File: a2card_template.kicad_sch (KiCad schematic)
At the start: 19 parts, among them U1 74LS00, U10 PLCCZ80, U14 74LS367, U15 74LS373, U16 74LS367, U17 74LS367, U3 74LS32, U5 74LS74, U6 74LS74, U7 74LS86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

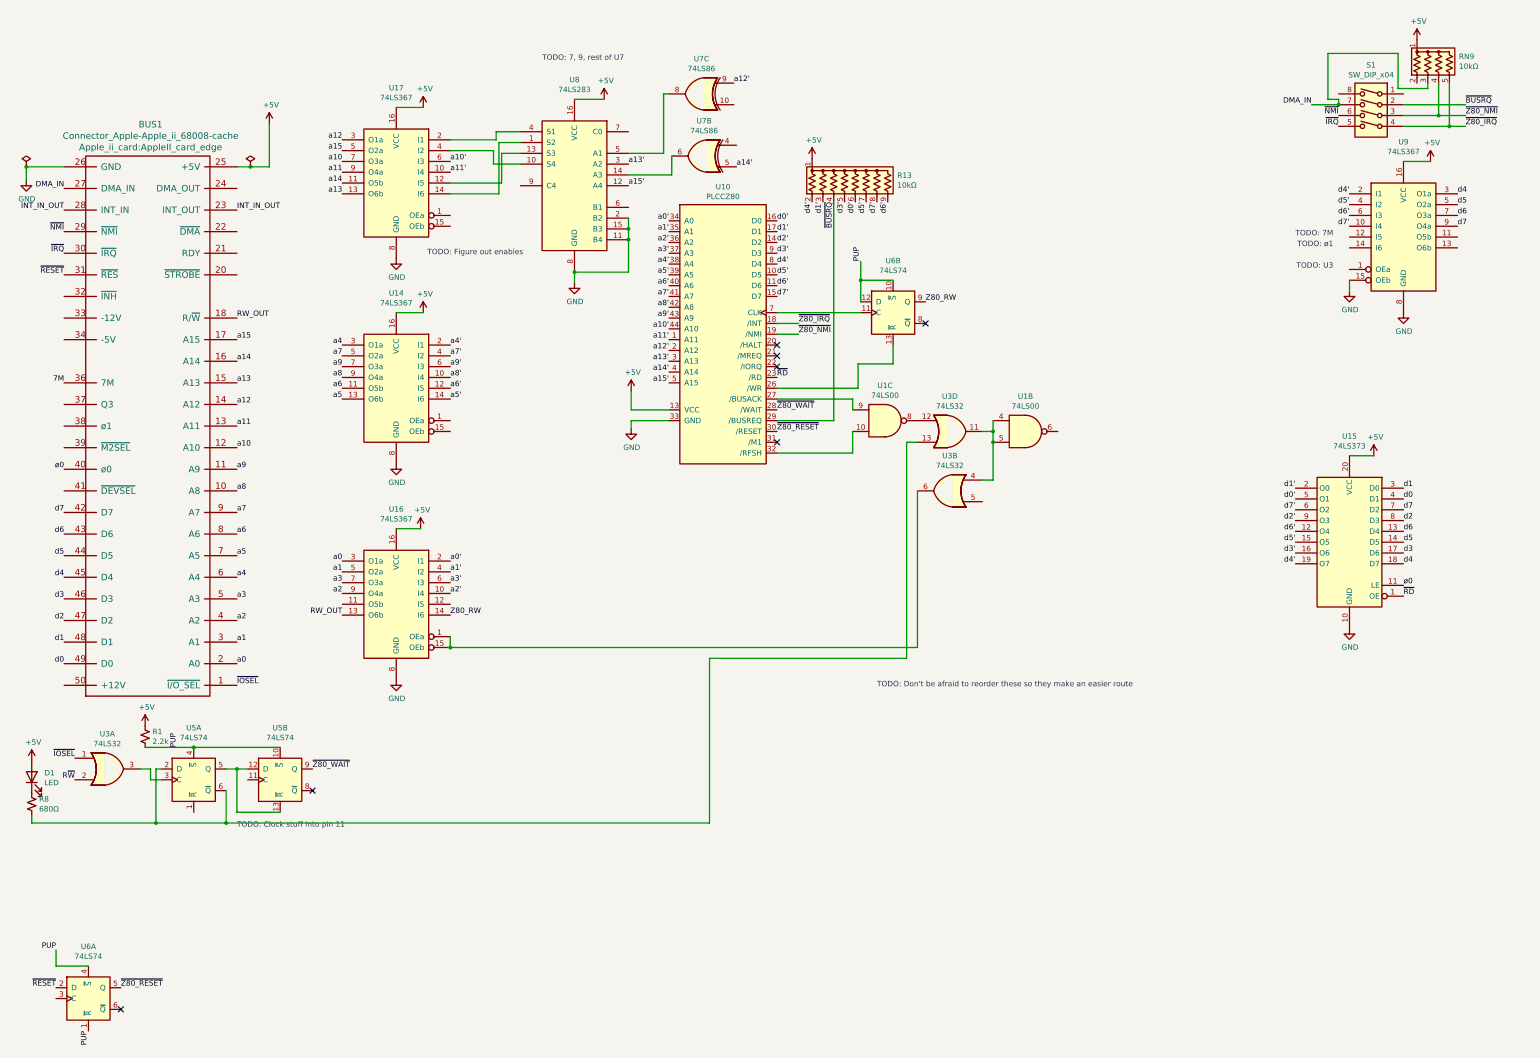
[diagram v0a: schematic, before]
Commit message: Add partial 74367 symbol, populate top row of schem
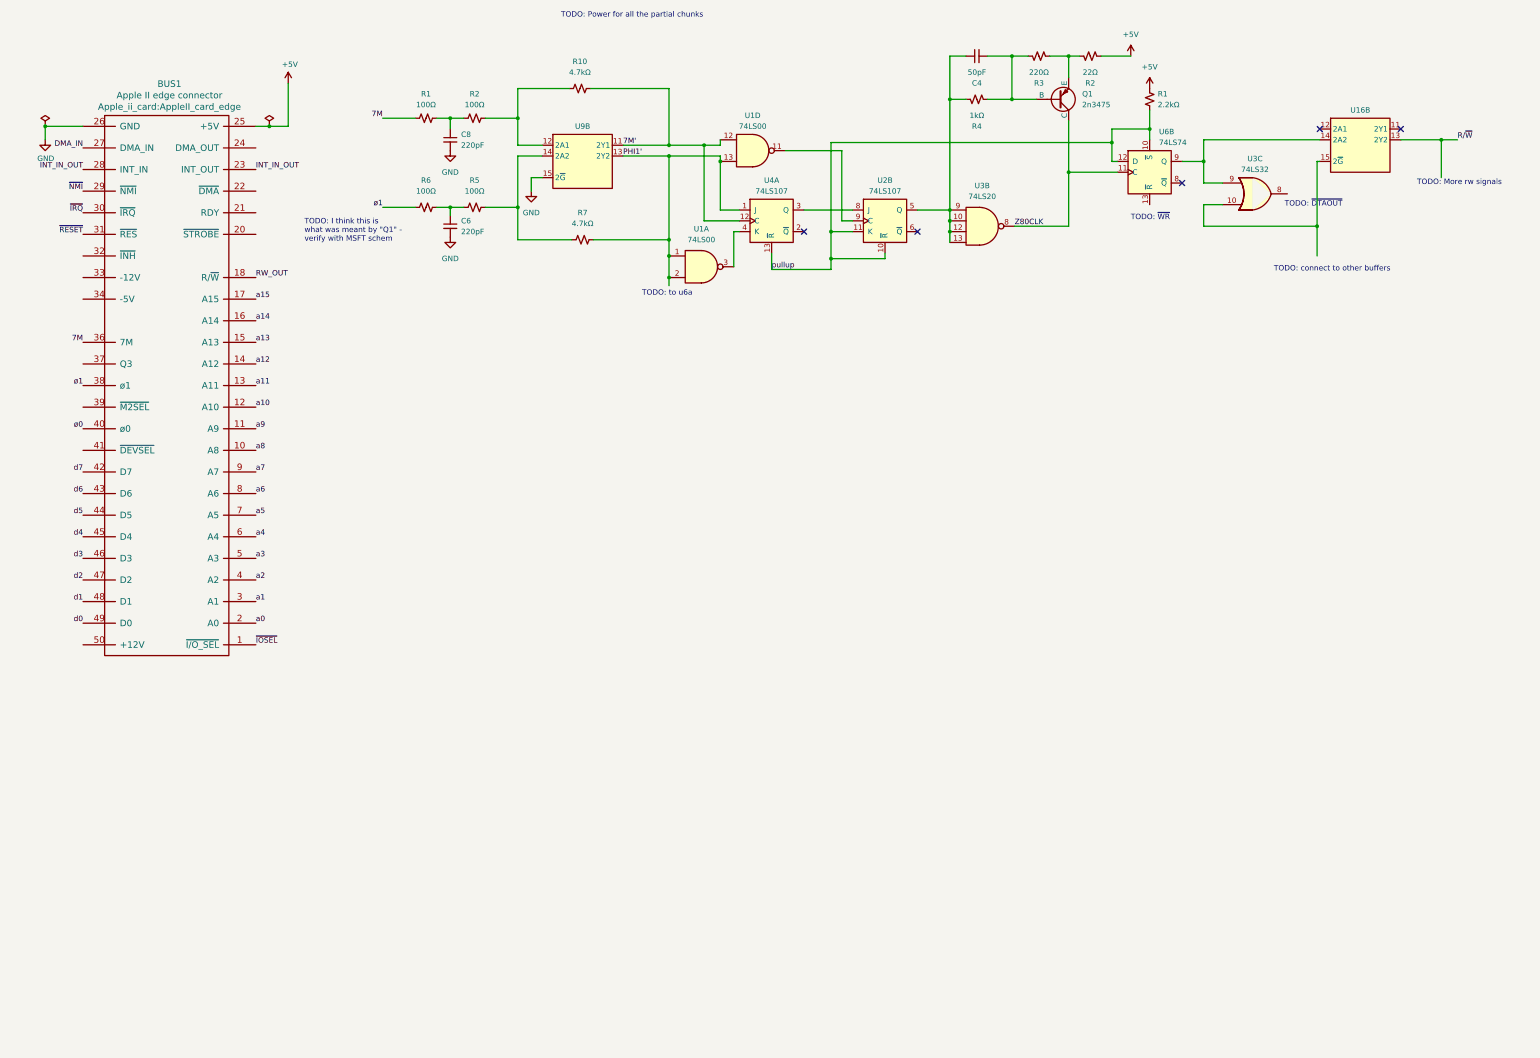
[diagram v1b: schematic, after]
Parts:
- removed D1: LED, LED_THT:LED_D5.0mm, symbol Device:LED
- removed R1: 2.2k, Resistor_THT:R_Axial_DIN0207_L6.3mm_D2.5mm_P7.62mm_Horizontal, symbol Device:R_Small_US
- removed R13: 10kΩ, Resistor_THT:R_Array_SIP9, symbol Device:R_Network08_US
- removed R8: 680Ω, Resistor_THT:R_Axial_DIN0207_L6.3mm_D2.5mm_P7.62mm_Horizontal, symbol Device:R_Small_US
- removed RN9: 10kΩ, Resistor_THT:R_Array_SIP5, symbol Device:R_Network04_US
- removed S1: SW_DIP_x04, Button_Switch_THT:SW_DIP_SPSTx04_Slide_9.78x12.34mm_W7.62mm_P2.54mm, symbol Switch:SW_DIP_x04
- removed U1: 74LS00, Package_DIP:DIP-14_W7.62mm, symbol 74xx:74LS00
- removed U10: PLCCZ80, Package_LCC:PLCC-44_THT-Socket, symbol LeadedSolder:PLCCZ80
- removed U14, U16, U17, U9: 74LS367, Package_DIP:DIP-16_W7.62mm, symbol 74xx:74LS367
- removed U15: 74LS373, Package_DIP:DIP-20_W7.62mm, symbol 74xx:74LS373
- removed U3: 74LS32, Package_DIP:DIP-14_W7.62mm, symbol 74xx:74LS32
- removed U5: 74LS74, Package_DIP:DIP-14_W7.62mm, symbol 74xx:74LS74
- removed unit 1 of U6
- removed U7: 74LS86, Package_DIP:DIP-14_W7.62mm, symbol 74xx:74LS86
- removed U8: 74LS283, Package_DIP:DIP-16_W7.62mm, symbol 74xx:74LS283
- added C4: 50pF, symbol Device:C_Small
- added C6, C8: 220pF, symbol Device:C_Small
- added Q1: 2n3475, symbol Simulation_SPICE:PNP
- added R1: 2.2kΩ, symbol Device:R_Small_US
- added R1, R2, R5, R6: 100Ω, symbol Device:R_Small_US
- added R10, R7: 4.7kΩ, symbol Device:R_Small_US
- added R2: 22Ω, symbol Device:R_Small_US
- added R3: 220Ω, symbol Device:R_Small_US
- added R4: 1kΩ, symbol Device:R_Small_US
- added U1: 74LS00, symbol 74xx:74LS00
- added U16, U9: ~, symbol Partial74s:74LS367
- added U2, U4: 74LS107, symbol 74xx:74LS107
- added U3: 74LS20, symbol 74xx:74LS20
- BUS1: value Connector_Apple-Apple_ii_68008-cache -> Apple II edge connector
- U6: footprint Package_DIP:DIP-14_W7.62mm -> (none)
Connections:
- net +5V: now also R1.1, R2.2
- net 7M: now also R1.1
- net GND: now also C6.2, C8.2, U9.15 (2~{G})
- net ø1: now reaches BUS1.38 (ø1)
- net ø1: now also R6.1
- net Z80CLK: now reaches U6.11 (C)
- net Z80CLK: now also Q1.1 (C), U3.8
- net PUP renamed pullup
- net pullup: now also R1.2, U2.10 (~{R}), U2.11 (K), U4.13 (~{R})
- net Z80_RW: no longer names the net of U6.9 (Q)
- net Z80_RW: now also U16.14 (2A2), U3.9
- new net: C4.1, R4.1, U2.5 (Q), U3.10, U3.12, U3.13, U3.9
- new net: C4.2, Q1.2 (B), R3.1, R4.2
- new net: U16.15 (2~{G}), U3.10
- new net: U2.8 (J), U4.3 (Q)
- new net: U1.11, U2.9 (C)
- new net: C6.1, R5.1, R6.2
- new net: R10.1, R2.2, U9.12 (2A1)
- new net: C8.1, R1.2, R2.1
- new net: Q1.3 (E), R2.1, R3.2
- new net: R5.2, R7.1, U9.14 (2A2)
- new net: U1.3, U4.4 (K)
- new net 7M': R10.2, U1.12, U4.12 (C), U9.11 (2Y1)
- new net PHI1': R7.2, U1.1, U1.13, U1.2, U4.1 (J), U9.13 (2Y2)
- new net R/~{W}: U16.13 (2Y2)
- no-connect marks 7 -> 5
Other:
- note added: "TODO: I think this is what was meant by "Q1" - verify with MSFT schem"
- note added: "TODO: More rw signals"
- note added: "TODO: Power for all the partial chunks"
- note added: "TODO: connect to other buffers"
- note added: "TODO: to u6a"
- note added: "TODO: ~{DTAOUT}"
- note added: "TODO: ~{WR}"
- note removed: "TODO: 7, 9, rest of U7"
- note removed: "TODO: 7M"
- note removed: "TODO: Clock stuff into pin 11"
- note removed: "TODO: Don't be afraid to reorder these so they make an easier route"
- note removed: "TODO: Figure out enables"
- note removed: "TODO: U3"
- note removed: "TODO: ø1"
- moved on the sheet: BUS1
